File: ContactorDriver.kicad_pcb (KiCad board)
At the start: 2 copper layers, 38.5 x 52.9 mm, 42 parts, among them J1 PowerConn, J10 FanConn3, J11 FanConn4, J2 DashboardConnA, J3 ContactorAConn, J4 DashboardConnB, J5 ContactorBConn, J6 DashboardConnC, J7 ContactorCConn, J8 FanConn1, J9 FanConn2, Q1 NDS356AP-VB, Q2 IRLML0030TRPbF, Q3 IRLML0030TRPbF, Q4 IRLML0030TRPbF

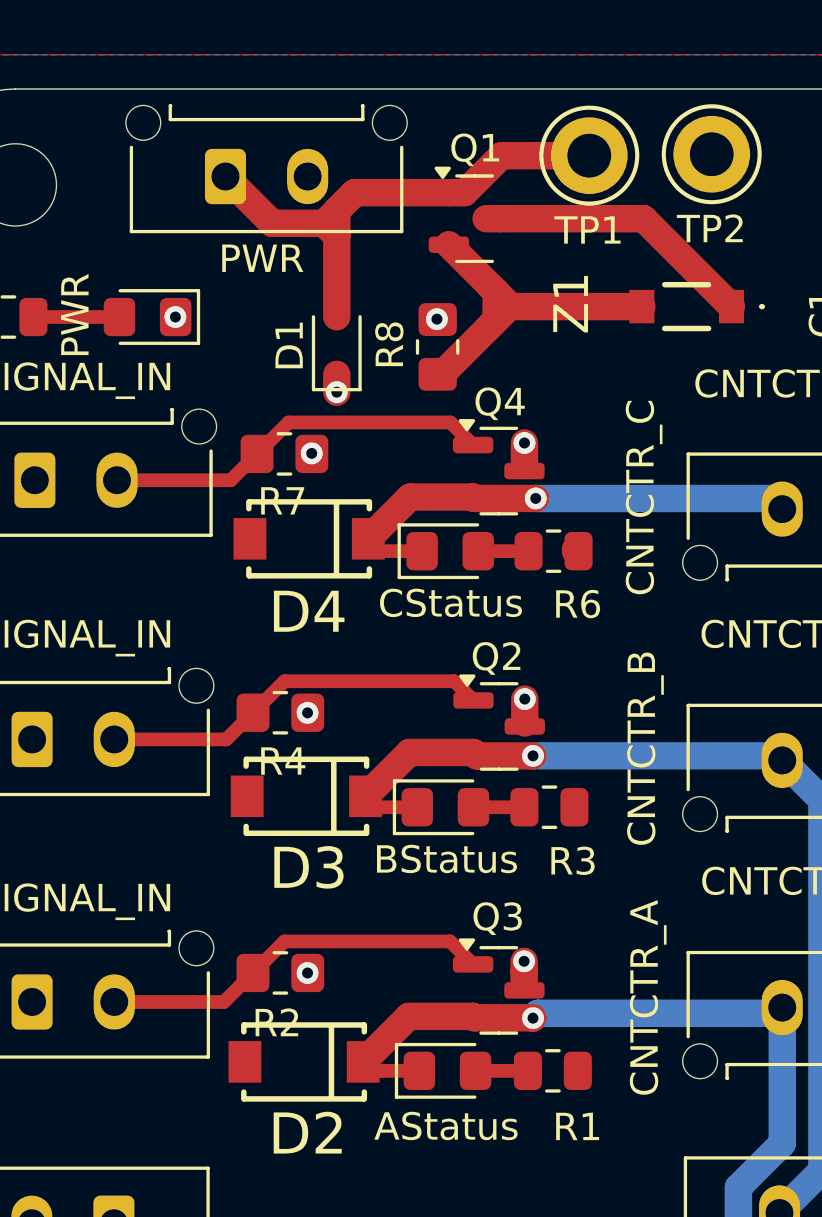
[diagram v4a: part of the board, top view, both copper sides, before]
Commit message: Fixed silkscreen
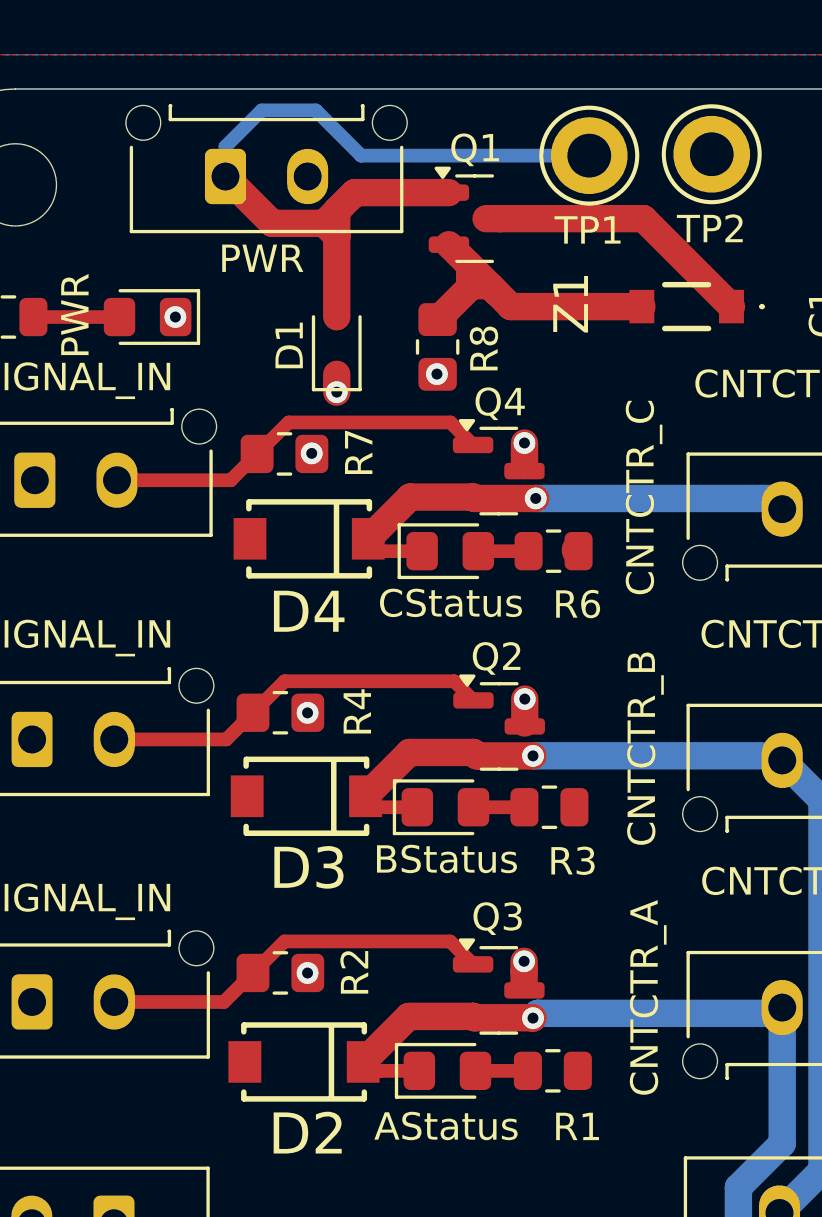
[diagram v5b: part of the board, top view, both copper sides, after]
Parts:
- turned R8 to 90 degrees
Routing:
- net Net-(D1-A2): track 20.5 -> 30.4 mm
- net Net-(Q1-G): track 13.4 -> 11.5 mm
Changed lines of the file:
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@@
 		(tags "resistor handsolder")
 		(property "Reference" "R2"
-			(at 0.125 -1.85 180)
+			(at -2.7456 0.0222 -90)
 			(layer "F.SilkS")
 			(effects
@@
 	(footprint "Resistor_SMD:R_0805_2012Metric_Pad1.20x1.40mm_HandSolder"
 		(layer "F.Cu")
-		(at 142.2178 92.5182 -90)
+		(at 142.2178 92.5182 90)
 		(descr "Resistor SMD 0805 (2012 Metric), square (rectangular) end terminal, IPC_7351 nominal with elongated pad for handsoldering. (Body size source: IPC-SM-782 page 72, https://www.pcb-3d.com/wordpress/wp-content/uploads/ipc-sm-782a_amendment_1_and_2.pdf), generated with kicad-footprint-generator")
 		(tags "resistor handsolder")
 		(property "Reference" "R8"
-			(at -0.0762 1.7272 90)
+			(at -0.0762 1.7272 270)
 			(layer "F.SilkS")
 			(effects
@@
 		)
 		(property "Value" "100k"
-			(at 0 1.65 90)
+			(at 0 1.65 270)
 			(layer "F.Fab")
 			(effects
@@
 		)
 		(property "Footprint" "Resistor_SMD:R_0805_2012Metric_Pad1.20x1.40mm_HandSolder"
-			(at 0 0 -90)
+			(at 0 0 90)
 			(unlocked yes)
 			(layer "F.Fab")
@@
 		)
 		(property "Datasheet" "https://www.mouser.com/datasheet/2/210/Kamaya_RMC_automotive_series_8_2022__1_-3032429.pdf"
-			(at 0 0 -90)
+			(at 0 0 90)
 			(unlocked yes)
 			(layer "F.Fab")
@@
 		)
 		(property "Description" ""
-			(at 0 0 -90)
+			(at 0 0 90)
 			(unlocked yes)
 			(layer "F.Fab")
@@
 		)
 		(property "P/N" "CRCW0805100KFKEAC"
-			(at 0 0 -90)
+			(at 0 0 90)
 			(unlocked yes)
 			(layer "F.Fab")
@@
 		(attr smd)
 		(fp_line
-			(start -0.227064 0.735)
-			(end 0.227064 0.735)
+			(start -0.227064 -0.735)
+			(end 0.227064 -0.735)
 			(stroke
 				(width 0.12)
@@
 		)
 		(fp_line
-			(start -0.227064 -0.735)
-			(end 0.227064 -0.735)
+			(start -0.227064 0.735)
+			(end 0.227064 0.735)
 			(stroke
 				(width 0.12)
@@
 		)
 		(fp_line
-			(start -1.85 0.95)
-			(end -1.85 -0.95)
+			(start 1.85 -0.95)
+			(end 1.85 0.95)
 			(stroke
 				(width 0.05)
@@
 		)
 		(fp_line
-			(start 1.85 0.95)
-			(end -1.85 0.95)
+			(start -1.85 -0.95)
+			(end 1.85 -0.95)
 			(stroke
 				(width 0.05)
@@
 		)
 		(fp_line
-			(start -1.85 -0.95)
-			(end 1.85 -0.95)
+			(start 1.85 0.95)
+			(end -1.85 0.95)
 			(stroke
 				(width 0.05)
@@
 		)
 		(fp_line
-			(start 1.85 -0.95)
-			(end 1.85 0.95)
+			(start -1.85 0.95)
+			(end -1.85 -0.95)
 			(stroke
 				(width 0.05)
@@
 		)
 		(fp_line
-			(start -1 0.625)
-			(end -1 -0.625)
+			(start 1 -0.625)
+			(end 1 0.625)
 			(stroke
 				(width 0.1)
@@
 		)
 		(fp_line
-			(start 1 0.625)
-			(end -1 0.625)
+			(start -1 -0.625)
+			(end 1 -0.625)
 			(stroke
 				(width 0.1)
@@
 		)
 		(fp_line
-			(start -1 -0.625)
-			(end 1 -0.625)
+			(start 1 0.625)
+			(end -1 0.625)
 			(stroke
 				(width 0.1)
@@
 		)
 		(fp_line
-			(start 1 -0.625)
-			(end 1 0.625)
+			(start -1 0.625)
+			(end -1 -0.625)
 			(stroke
 				(width 0.1)
@@
 		)
 		(fp_text user "${REFERENCE}"
-			(at 0 0 90)
+			(at 0 0 270)
 			(layer "F.Fab")
 			(effects
@@
 		)
 		(pad "1" smd roundrect
-			(at -1 0 270)
+			(at -1 0 90)
 			(size 1.2 1.4)
 			(layers "F.Cu" "F.Paste" "F.Mask")
@@
 		)
 		(pad "2" smd roundrect
-			(at 1 0 270)
+			(at 1 0 90)
 			(size 1.2 1.4)
 			(layers "F.Cu" "F.Paste" "F.Mask")
@@
 		(tags "resistor handsolder")
 		(property "Reference" "R7"
-			(at 0.075 -1.75 180)
+			(at -2.748 0.046 -90)
 			(layer "F.SilkS")
 			(effects
@@
 		(tags "resistor handsolder")
 		(property "Reference" "R4"
-			(at -0.075 -1.8 180)
+			(at -2.8472 0.0218 -90)
 			(layer "F.SilkS")
 			(effects
@@
 	)
 	(segment
+		(start 142.2272 93.5182)
+		(end 142.36823 93.5182)
+		(width 1)
+		(layer "F.Cu")
+		(net 2)
+	)
+	(segment
 		(start 145.3875 96.438)
 		(end 145.3875 97.05)
@@
 	)
 	(segment
+		(start 142.2178 93.5182)
+		(end 142.2084 93.5182)
+		(width 1)
+		(layer "F.Cu")
+		(net 2)
+	)
+	(segment
 		(start 145.388 96.025)
 		(end 145.388 96.4375)
@@
 	)
 	(segment
+		(start 142.1924 93.5088)
+		(end 142.2272 93.5182)
+		(width 1)
+		(layer "F.Cu")
+		(net 2)
+	)
+	(segment
 		(start 138.5348 93.5174)
 		(end 138.5348 94.1692)
@@
 	)
 	(segment
+		(start 142.2084 93.5182)
+		(end 142.1924 93.5088)
+		(width 1)
+		(layer "F.Cu")
+		(net 2)
+	)
+	(segment
 		(start 145.4 105.375)
 		(end 145.4 106.25)
@@
 	)
 	(via
-		(at 137.6204 96.4044)
+		(at 142.1924 93.5088)
 		(size 0.8)
 		(drill 0.4)
@@
 	)
 	(via
-		(at 142.1924 91.5022)
+		(at 137.6204 96.4044)
 		(size 0.8)
 		(drill 0.4)
@@
 	)
 	(segment
-		(start 144.5546 85.5332)
-		(end 147.755 85.5332)
-		(width 1)
-		(layer "F.Cu")
-		(net 13)
-	)
-	(segment
-		(start 143.2034 86.8844)
-		(end 144.5546 85.5332)
-		(width 1)
-		(layer "F.Cu")
-		(net 13)
-	)
-	(segment
 		(start 139.19221 86.8844)
 		(end 138.07141 88.0052)
@@
 	)
 	(segment
-		(start 142.6288 86.8844)
-		(end 143.2034 86.8844)
-		(width 1)
-		(layer "F.Cu")
+		(start 134.4708 85.203)
+		(end 135.7916 83.8822)
+		(width 0.5)
+		(layer "B.Cu")
 		(net 13)
 	)
 	(segment
-		(start 144.3537 90.5093)
-		(end 144.3537 91.53273)
+		(start 139.4238 85.5332)
+		(end 147.755 85.5332)
+		(width 0.5)
+		(layer "B.Cu")
+		(net 13)
+	)
+	(segment
+		(start 137.7728 83.8822)
+		(end 139.4238 85.5332)
+		(width 0.5)
+		(layer "B.Cu")
+		(net 13)
+	)
+	(segment
+		(start 135.7916 83.8822)
+		(end 137.7728 83.8822)
+		(width 0.5)
+		(layer "B.Cu")
+		(net 13)
+	)
+	(segment
+		(start 134.4708 86.2952)
+		(end 134.4708 85.203)
+		(width 0.5)
+		(layer "B.Cu")
+		(net 13)
+	)
+	(segment
+		(start 143.3885 89.5441)
+		(end 142.6288 88.7844)
 		(width 1)
 		(layer "F.Cu")
@@
 	)
 	(segment
-		(start 144.84143 91.045)
-		(end 144.8894 91.045)
+		(start 144.1632 90.3188)
+		(end 143.3885 89.5441)
 		(width 1)
 		(layer "F.Cu")
@@
 	)
 	(segment
-		(start 144.8894 91.045)
-		(end 144.1632 90.3188)
+		(start 143.3885 90.2139)
+		(end 143.3885 89.5441)
 		(width 1)
 		(layer "F.Cu")
@@
 	)
 	(segment
-		(start 142.2178 93.5182)
-		(end 142.36823 93.5182)
+		(start 144.8894 91.045)
+		(end 144.1632 90.3188)
 		(width 1)
 		(layer "F.Cu")
@@
 	)
 	(segment
-		(start 144.075715 91.810715)
-		(end 144.84143 91.045)
+		(start 144.1251 90.2807)
+		(end 143.4553 90.2807)
 		(width 1)
 		(layer "F.Cu")
@@
 	)
 	(segment
-		(start 144.1632 90.3188)
-		(end 142.6288 88.7844)
+		(start 143.4553 90.2807)
+		(end 142.2178 91.5182)
 		(width 1)
 		(layer "F.Cu")
@@
 	)
 	(segment
-		(start 144.3537 91.53273)
-		(end 144.075715 91.810715)
+		(start 144.1632 90.3188)
+		(end 144.1251 90.2807)
 		(width 1)
 		(layer "F.Cu")
@@
 	)
 	(segment
-		(start 142.36823 93.5182)
-		(end 144.075715 91.810715)
+		(start 143.4553 90.2807)
+		(end 143.3885 90.2139)
 		(width 1)
 		(layer "F.Cu")

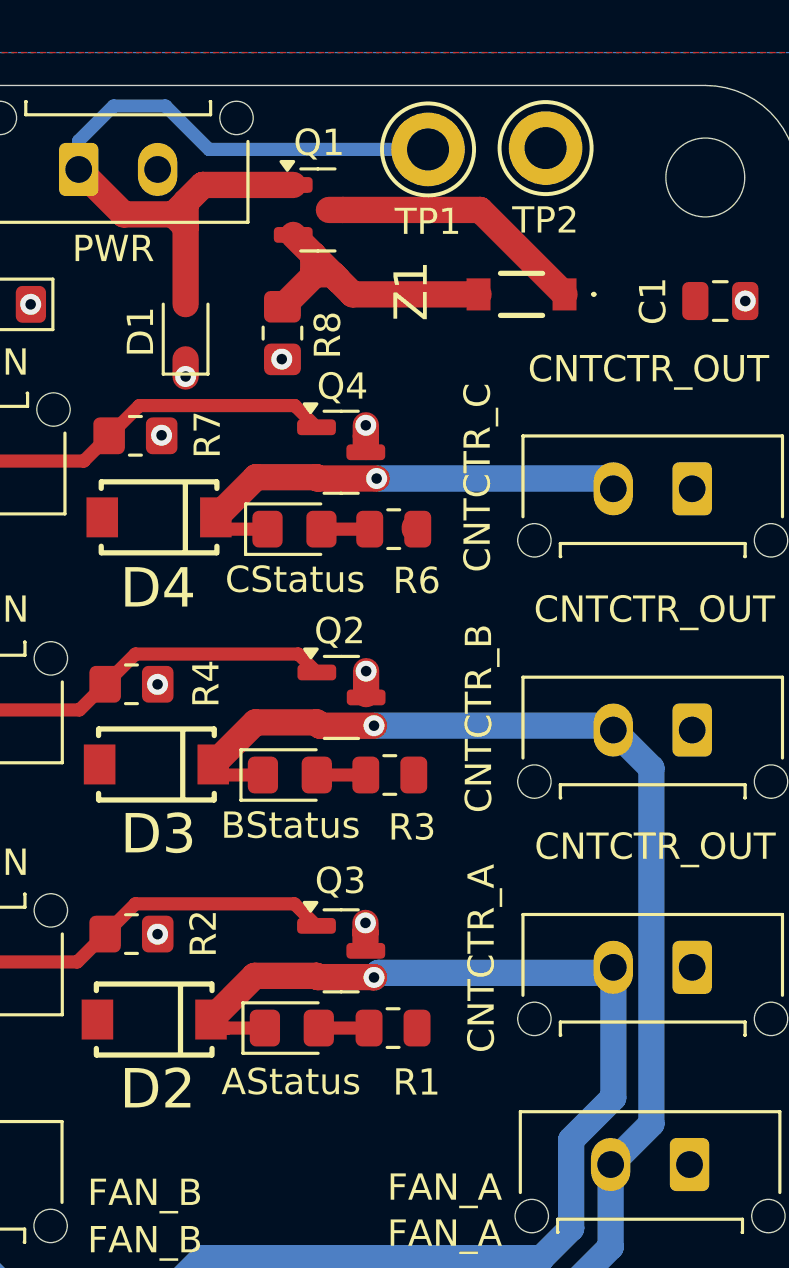
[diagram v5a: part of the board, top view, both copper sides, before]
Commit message: Updated BOM, PDFs, and added labels for tps
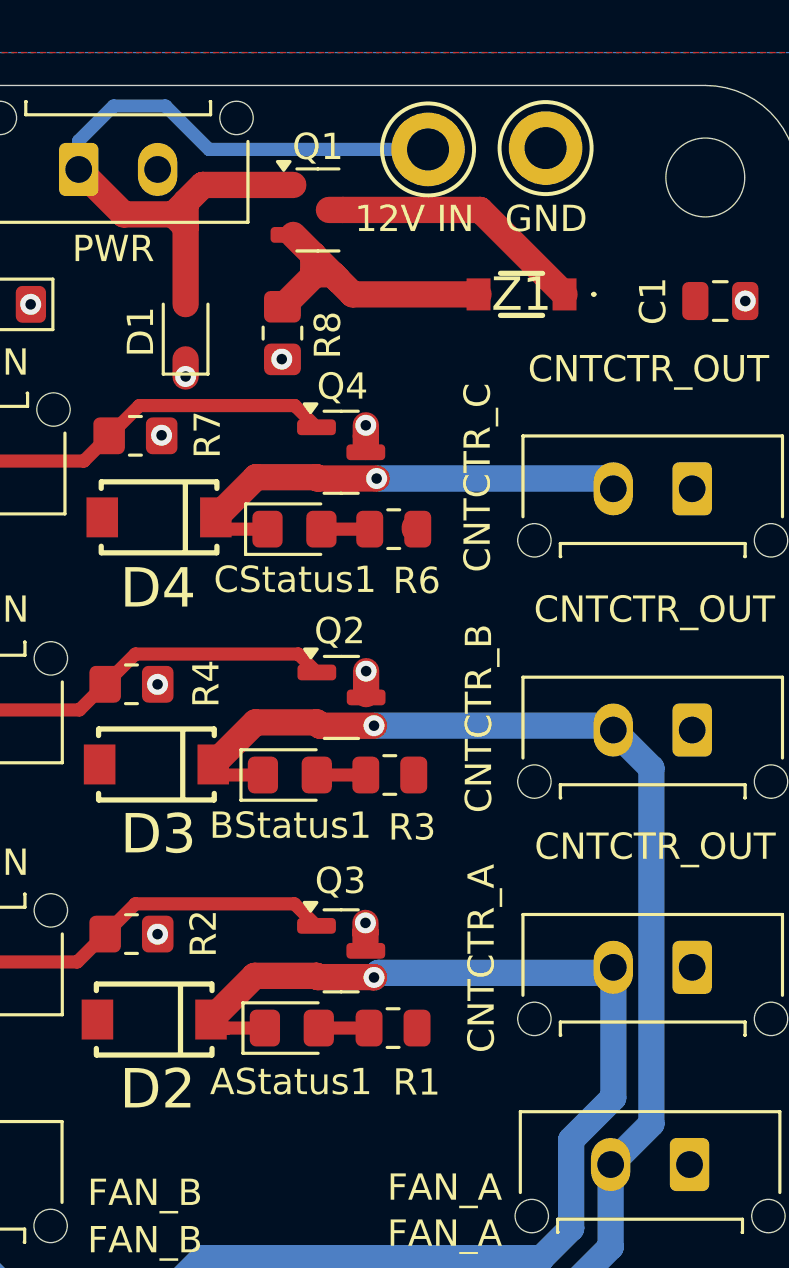
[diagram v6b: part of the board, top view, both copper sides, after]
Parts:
- added LOGO4: UTSVT, UTSVT_Special:UTSVT_Logo_Symbol, B.Cu at (138.2, 91.0)
- Q1: value NDS356AP-VB -> PMV35EPER; footprint Package_TO_SOT_SMD:SOT-23 -> Package_TO_SOT_SMD:SOT-23-3
- renumbered AStatus to AStatus1, BStatus to BStatus1, CStatus to CStatus1
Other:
- board text added: "12V IN"
- board text added: "GND"

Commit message: layout changes
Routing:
- net /CONTACTOR_A_V-: track 59.6 -> 18.4 mm, vias 1 -> 2
- net /CONTACTOR_B_V-: track 48.2 -> 35.8 mm
- net Net-(Q1-G): track 11.5 -> 10.6 mm, vias 0 -> 3
- added copper zone on B.Cu, net /CONTACTOR_A_V-
- added copper zone on B.Cu, net /CONTACTOR_B_V-
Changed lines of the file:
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@@
+	)
+	(segment
+		(start 139.55 118.65)
+		(end 139.525 118.65)
+		(width 0.5)
+		(layer "F.Cu")
+		(net 5)
 	)
 	(segment
@@
 	)
 	(segment
+		(start 139.55 118.675)
+		(end 139.55 118.65)
+		(width 0.5)
+		(layer "F.Cu")
+		(net 5)
+	)
+	(segment
 		(start 140.1258 118.95)
 		(end 139.825 118.95)
@@
 	)
 	(segment
+		(start 139.525 118.65)
+		(end 139.5 118.625)
+		(width 0.5)
+		(layer "F.Cu")
+		(net 5)
+	)
+	(segment
 		(start 139.5 118.625)
 		(end 141.162 116.962)
@@
 	(segment
 		(start 139.825 118.95)
-		(end 139.5 118.625)
+		(end 139.55 118.675)
 		(width 0.5)
 		(layer "F.Cu")
@@
 		(net 5)
 	)
+	(via
+		(at 139.55 118.65)
+		(size 0.8)
+		(drill 0.4)
+		(layers "F.Cu" "B.Cu")
+		(net 5)
+	)
 	(segment
 		(start 145.7 117.025)
@@
 	)
 	(segment
-		(start 138.11457 128.775)
-		(end 135.48957 131.4)
-		(width 1)
-		(layer "B.Cu")
-		(net 5)
-	)
-	(segment
-		(start 138.11457 128.76043)
-		(end 138.11457 128.775)
-		(width 1)
-		(layer "B.Cu")
-		(net 5)
-	)
-	(segment
-		(start 153.2 126.564343)
-		(end 152.064343 127.7)
-		(width 1)
-		(layer "B.Cu")
-		(net 5)
-	)
-	(segment
-		(start 134.285 131.4)
-		(end 127.4 124.515)
-		(width 1)
-		(layer "B.Cu")
-		(net 5)
-	)
-	(segment
-		(start 154.8 121.6)
-		(end 153.2 123.2)
-		(width 1)
-		(layer "B.Cu")
-		(net 5)
-	)
-	(segment
-		(start 139.175 127.7)
-		(end 138.11457 128.76043)
-		(width 1)
-		(layer "B.Cu")
-		(net 5)
-	)
-	(segment
 		(start 154.59 116.85)
 		(end 154.8 116.64)
@@
 	)
 	(segment
-		(start 135.48957 131.4)
-		(end 135.1 131.4)
-		(width 1)
-		(layer "B.Cu")
-		(net 5)
-	)
-	(segment
-		(start 153.2 123.2)
-		(end 153.2 126.564343)
-		(width 1)
-		(layer "B.Cu")
-		(net 5)
-	)
-	(segment
-		(start 152.064343 127.7)
-		(end 139.175 127.7)
-		(width 1)
-		(layer "B.Cu")
-		(net 5)
-	)
-	(segment
-		(start 135.1 131.4)
-		(end 134.285 131.4)
-		(width 1)
-		(layer "B.Cu")
-		(net 5)
-	)
-	(segment
 		(start 145.875 116.85)
 		(end 154.59 116.85)
-		(width 1)
-		(layer "B.Cu")
-		(net 5)
-	)
-	(segment
-		(start 154.8 116.64)
-		(end 154.8 121.6)
 		(width 1)
 		(layer "B.Cu")
@@
 	)
 	(segment
-		(start 149.265 129.15)
-		(end 147.1 131.315)
-		(width 1)
-		(layer "B.Cu")
-		(net 7)
-	)
-	(segment
-		(start 154.7 127.275)
-		(end 152.825 129.15)
-		(width 1)
-		(layer "B.Cu")
-		(net 7)
-	)
-	(segment
 		(start 154.8 107.615)
 		(end 156.25 109.065)
@@
 	)
 	(segment
-		(start 154.7 124.14)
-		(end 154.7 127.275)
-		(width 1)
-		(layer "B.Cu")
-		(net 7)
-	)
-	(segment
 		(start 145.7 107.45)
 		(end 154.635 107.45)
-		(width 1)
-		(layer "B.Cu")
-		(net 7)
-	)
-	(segment
-		(start 152.825 129.15)
-		(end 149.265 129.15)
 		(width 1)
 		(layer "B.Cu")
@@
 	)
 	(segment
+		(start 138.2322 83.8822)
+		(end 139.8832 85.5332)
+		(width 0.5)
+		(layer "B.Cu")
+		(net 13)
+	)
+	(segment
+		(start 135.7916 83.8822)
+		(end 138.2322 83.8822)
+		(width 0.5)
+		(layer "B.Cu")
+		(net 13)
+	)
+	(segment
 		(start 134.4708 85.203)
 		(end 135.7916 83.8822)
@@
 	)
 	(segment
-		(start 139.4238 85.5332)
+		(start 139.8832 85.5332)
 		(end 147.755 85.5332)
-		(width 0.5)
-		(layer "B.Cu")
-		(net 13)
-	)
-	(segment
-		(start 137.7728 83.8822)
-		(end 139.4238 85.5332)
-		(width 0.5)
-		(layer "B.Cu")
-		(net 13)
-	)
-	(segment
-		(start 135.7916 83.8822)
-		(end 137.7728 83.8822)
 		(width 0.5)
 		(layer "B.Cu")
@@
 	)
 	(segment
-		(start 143.3885 89.5441)
-		(end 142.6288 88.7844)
-		(width 1)
-		(layer "F.Cu")
-		(net 14)
-	)
-	(segment
-		(start 144.1632 90.3188)
-		(end 143.3885 89.5441)
-		(width 1)
-		(layer "F.Cu")
-		(net 14)
-	)
-	(segment
-		(start 143.3885 90.2139)
-		(end 143.3885 89.5441)
-		(width 1)
-		(layer "F.Cu")
-		(net 14)
-	)
-	(segment
-		(start 144.8894 91.045)
-		(end 144.1632 90.3188)
-		(width 1)
-		(layer "F.Cu")
-		(net 14)
-	)
-	(segment
-		(start 144.1251 90.2807)
-		(end 143.4553 90.2807)
-		(width 1)
-		(layer "F.Cu")
-		(net 14)
-	)
-	(segment
-		(start 144.1632 90.3188)
-		(end 144.3537 90.5093)
-		(width 1)
-		(layer "F.Cu")
-		(net 14)
-	)
-	(segment
-		(start 143.4553 90.2807)
-		(end 142.2178 91.5182)
-		(width 1)
-		(layer "F.Cu")
-		(net 14)
-	)
-	(segment
-		(start 149.676 91.045)
-		(end 144.8894 91.045)
-		(width 1)
-		(layer "F.Cu")
-		(net 14)
-	)
-	(segment
-		(start 144.1632 90.3188)
-		(end 144.1251 90.2807)
-		(width 1)
-		(layer "F.Cu")
-		(net 14)
-	)
-	(segment
-		(start 143.4553 90.2807)
-		(end 143.3885 90.2139)
-		(width 1)
-		(layer "F.Cu")
+		(start 143.275 89.625)
+		(end 142.4344 88.7844)
+		(width 1)
+		(layer "F.Cu")
+		(net 14)
+	)
+	(segment
+		(start 142.2 91.5)
+		(end 142.25 91.5)
+		(width 1)
+		(layer "F.Cu")
+		(net 14)
+	)
+	(segment
+		(start 142.4344 88.7844)
+		(end 142.4288 88.7844)
+		(width 1)
+		(layer "F.Cu")
+		(net 14)
+	)
+	(via
+		(at 149.7 91.05)
+		(size 0.8)
+		(drill 0.4)
+		(layers "F.Cu" "B.Cu")
+		(net 14)
+	)
+	(via
+		(at 143.275 89.625)
+		(size 0.8)
+		(drill 0.4)
+		(layers "F.Cu" "B.Cu")
+		(net 14)
+	)
+	(via
+		(at 142.2 91.5)
+		(size 0.8)
+		(drill 0.4)
+		(layers "F.Cu" "B.Cu")
+		(net 14)
+	)
+	(segment
+		(start 142.25 91.5)
+		(end 143.275 90.475)
+		(width 1)
+		(layer "B.Cu")
+		(net 14)
+	)
+	(segment
+		(start 144.7 91.05)
+		(end 149.7 91.05)
+		(width 1)
+		(layer "B.Cu")
+		(net 14)
+	)
+	(segment
+		(start 143.275 90.475)
+		(end 143.275 89.625)
+		(width 1)
+		(layer "B.Cu")
+		(net 14)
+	)
+	(segment
+		(start 143.275 89.625)
+		(end 144.7 91.05)
+		(width 1)
+		(layer "B.Cu")
 		(net 14)
 	)
@@
 	)
 	(zone
-		(net 2)
-		(net_name "GND")
+		(net 7)
+		(net_name "/CONTACTOR_B_V-")
 		(layer "B.Cu")
 		(hatch edge 0.5)
-		(priority 1)
+		(priority 2)
 		(connect_pads
 			(clearance 0.2)
@@
 		(polygon
 			(pts
+				(xy 143.3 134.25) (xy 156.4 134.25) (xy 156.4 122.05) (xy 150.9 122.05) (xy 150.9 129.05) (xy 143.3 129.05)
+			)
+		)
+	)
+	(zone
+		(net 2)
+		(net_name "GND")
+		(layer "B.Cu")
+		(hatch edge 0.5)
+		(priority 1)
+		(connect_pads
+			(clearance 0.2)
+		)
+		(min_thickness 0.25)
+		(filled_areas_thickness no)
+		(fill yes
+			(thermal_gap 0.5)
+			(thermal_bridge_width 0.5)
+		)
+		(polygon
+			(pts
 				(xy 163.05 81.85) (xy 122.05 81.85) (xy 121.8 82.1) (xy 121.8 136.85) (xy 163.05 136.85)
 			)
 		)
+	)
+	(zone
+		(net 5)
+		(net_name "/CONTACTOR_A_V-")
+		(layer "B.Cu")
+		(hatch edge 0.5)
+		(priority 3)
+		(connect_pads
+			(clearance 0.2)
+		)
+		(min_thickness 0.25)
+		(filled_areas_thickness no)
+		(fill yes
+			(thermal_gap 0.5)
+			(thermal_bridge_width 0.5)
+		)
+		(polygon
+			(pts
+				(xy 140.45 134.35) (xy 140.45 117.9) (xy 124.65 117.9) (xy 124.65 124.45) (xy 134.55 134.35)
+			)
+		)
